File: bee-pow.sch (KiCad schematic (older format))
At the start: 41 parts, among them J1 Conn_01x02_Male, J2 Conn_01x02_Male, J3 Conn_01x02_Male, J4 Conn_01x02_Male, J5 Screw_Terminal_01x03, J6 Screw_Terminal_01x02, U1 L7805, U2 L7815, U3 L7915

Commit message: schematic and layout
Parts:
- removed D10, D12, D15: 1N4001, Diode_THT:D_A-405_P12.70mm_Horizontal, symbol Diode:1N4001
- removed D4, D7, D8: D_Schottky, Diode_THT:D_A-405_P10.16mm_Horizontal, symbol Device:D_Schottky
- removed J5: Screw_Terminal_01x03, TerminalBlock:TerminalBlock_bornier-3_P5.08mm, symbol Connector:Screw_Terminal_01x03
- removed J6: Screw_Terminal_01x02, TerminalBlock:TerminalBlock_bornier-2_P5.08mm, symbol Connector:Screw_Terminal_01x02
- added J5: Screw_Terminal_01x04, TerminalBlock:TerminalBlock_bornier-4_P5.08mm, symbol Connector:Screw_Terminal_01x04
- C7, C8, C9: footprint Capacitor_THT:CP_Radial_D10.0mm_P5.00mm -> Capacitor_THT:CP_Radial_D8.0mm_P2.50mm; order number RAD 220/35 -> RND 150ECR AZ
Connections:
- net labels added: U3_1
- wire segments 126 -> 125
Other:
- note removed: "Alternativ \nSMD oder DIL"
- moved on the sheet: D2, JP1

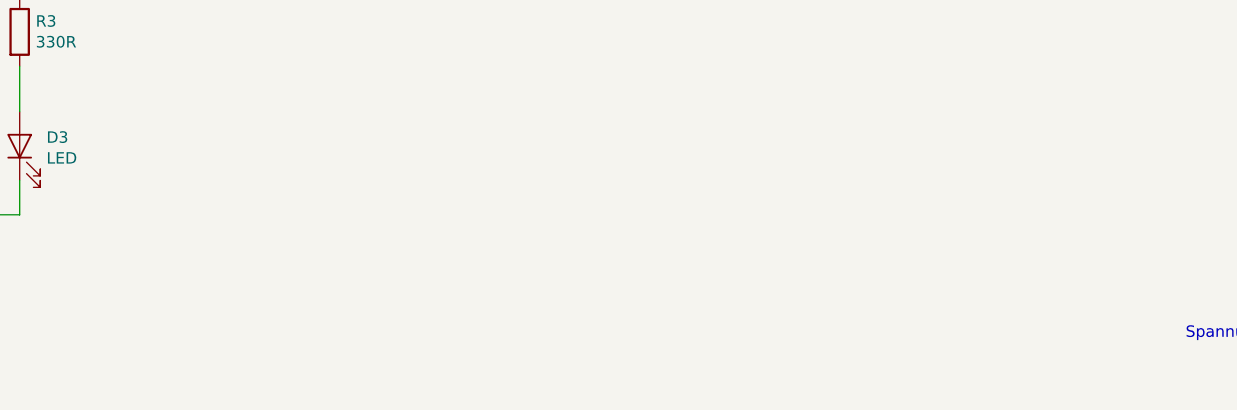
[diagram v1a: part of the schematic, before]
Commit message: Update labels and mounting holes.
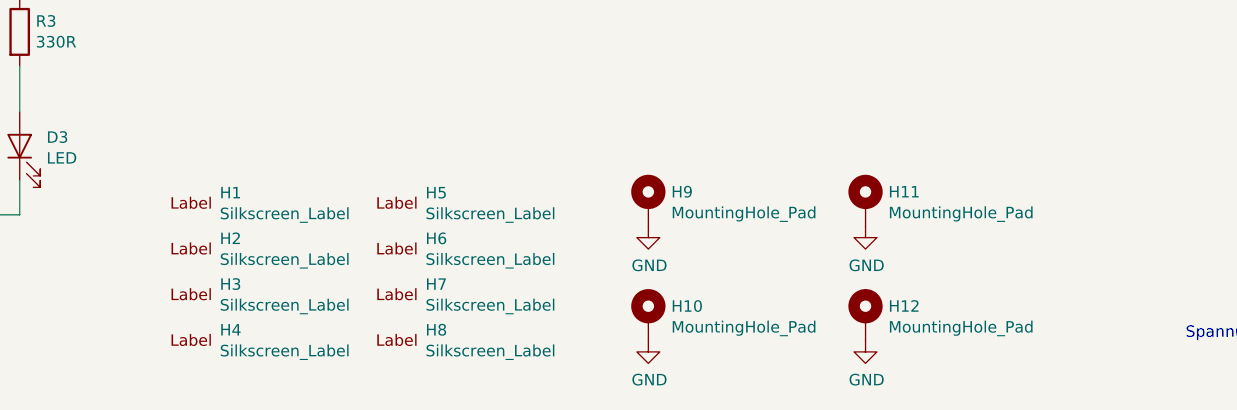
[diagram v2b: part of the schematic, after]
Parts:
- added H1, H2: Silkscreen_Label, Symbol-emt:Text_U_B+_Silkscreen, symbol Mechanical-emt:Silkscreen_Label
- added H10, H11, H12, H9: MountingHole_Pad, MountingHole:MountingHole_3.2mm_M3_ISO7380_Pad, symbol Mechanical:MountingHole_Pad
- added H3, H4: Silkscreen_Label, Symbol-emt:Text_U_B-_Silkscreen, symbol Mechanical-emt:Silkscreen_Label
- added H5, H6: Silkscreen_Label, Symbol-emt:Text_U_B2_Silkscreen, symbol Mechanical-emt:Silkscreen_Label
- added H7, H8: Silkscreen_Label, Symbol-emt:Symbol_GND_Silkscreen, symbol Mechanical-emt:Silkscreen_Label
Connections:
- net GND: now also H10.1, H11.1, H12.1, H9.1
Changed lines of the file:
@@
 Wire Wire Line
 	1800 6950 1800 6800
+$Comp
+L Mechanical-emt:Silkscreen_Label H1
+U 1 1 5CC84E73
+P 3000 6900
+F 0 "H1" H 3125 6945 50  0000 L CNN
+F 1 "Silkscreen_Label" H 3125 6854 50  0000 L CNN
+F 2 "Symbol-emt:Text_U_B+_Silkscreen" H 3000 6900 50  0001 C CNN
+F 3 "~" H 3000 6900 50  0001 C CNN
+	1    3000 6900
+	1    0    0    -1
+$EndComp
+$Comp
+L Mechanical-emt:Silkscreen_Label H2
+U 1 1 5CC86235
+P 3000 7100
+F 0 "H2" H 3125 7145 50  0000 L CNN
+F 1 "Silkscreen_Label" H 3125 7054 50  0000 L CNN
+F 2 "Symbol-emt:Text_U_B+_Silkscreen" H 3000 7100 50  0001 C CNN
+F 3 "~" H 3000 7100 50  0001 C CNN
+	1    3000 7100
+	1    0    0    -1
+$EndComp
+$Comp
+L Mechanical-emt:Silkscreen_Label H3
+U 1 1 5CC865CE
+P 3000 7300
+F 0 "H3" H 3125 7345 50  0000 L CNN
+F 1 "Silkscreen_Label" H 3125 7254 50  0000 L CNN
+F 2 "Symbol-emt:Text_U_B-_Silkscreen" H 3000 7300 50  0001 C CNN
+F 3 "~" H 3000 7300 50  0001 C CNN
+	1    3000 7300
+	1    0    0    -1
+$EndComp
+$Comp
+L Mechanical-emt:Silkscreen_Label H4
+U 1 1 5CC8C4D2
+P 3000 7500
+F 0 "H4" H 3125 7545 50  0000 L CNN
+F 1 "Silkscreen_Label" H 3125 7454 50  0000 L CNN
+F 2 "Symbol-emt:Text_U_B-_Silkscreen" H 3000 7500 50  0001 C CNN
+F 3 "~" H 3000 7500 50  0001 C CNN
+	1    3000 7500
+	1    0    0    -1
+$EndComp
+$Comp
+L Mechanical-emt:Silkscreen_Label H5
+U 1 1 5CC8C802
+P 3900 6900
+F 0 "H5" H 4025 6945 50  0000 L CNN
+F 1 "Silkscreen_Label" H 4025 6854 50  0000 L CNN
+F 2 "Symbol-emt:Text_U_B2_Silkscreen" H 3900 6900 50  0001 C CNN
+F 3 "~" H 3900 6900 50  0001 C CNN
+	1    3900 6900
+	1    0    0    -1
+$EndComp
+$Comp
+L Mechanical-emt:Silkscreen_Label H6
+U 1 1 5CC8CC95
+P 3900 7100
+F 0 "H6" H 4025 7145 50  0000 L CNN
+F 1 "Silkscreen_Label" H 4025 7054 50  0000 L CNN
+F 2 "Symbol-emt:Text_U_B2_Silkscreen" H 3900 7100 50  0001 C CNN
+F 3 "~" H 3900 7100 50  0001 C CNN
+	1    3900 7100
+	1    0    0    -1
+$EndComp
+$Comp
+L Mechanical-emt:Silkscreen_Label H7
+U 1 1 5CC8CECB
+P 3900 7300
+F 0 "H7" H 4025 7345 50  0000 L CNN
+F 1 "Silkscreen_Label" H 4025 7254 50  0000 L CNN
+F 2 "Symbol-emt:Symbol_GND_Silkscreen" H 3900 7300 50  0001 C CNN
+F 3 "~" H 3900 7300 50  0001 C CNN
+	1    3900 7300
+	1    0    0    -1
+$EndComp
+$Comp
+L Mechanical-emt:Silkscreen_Label H8
+U 1 1 5CC8D0ED
+P 3900 7500
+F 0 "H8" H 4025 7545 50  0000 L CNN
+F 1 "Silkscreen_Label" H 4025 7454 50  0000 L CNN
+F 2 "Symbol-emt:Symbol_GND_Silkscreen" H 3900 7500 50  0001 C CNN
+F 3 "~" H 3900 7500 50  0001 C CNN
+	1    3900 7500
+	1    0    0    -1
+$EndComp
+$Comp
+L Mechanical:MountingHole_Pad H9
+U 1 1 5CC913F6
+P 5000 6900
+F 0 "H9" H 5100 6949 50  0000 L CNN
+F 1 "MountingHole_Pad" H 5100 6858 50  0000 L CNN
+F 2 "MountingHole:MountingHole_3.2mm_M3_ISO7380_Pad" H 5000 6900 50  0001 C CNN
+F 3 "~" H 5000 6900 50  0001 C CNN
+	1    5000 6900
+	1    0    0    -1
+$EndComp
+$Comp
+L Mechanical:MountingHole_Pad H10
+U 1 1 5CC9212B
+P 5000 7400
+F 0 "H10" H 5100 7449 50  0000 L CNN
+F 1 "MountingHole_Pad" H 5100 7358 50  0000 L CNN
+F 2 "MountingHole:MountingHole_3.2mm_M3_ISO7380_Pad" H 5000 7400 50  0001 C CNN
+F 3 "~" H 5000 7400 50  0001 C CNN
+	1    5000 7400
+	1    0    0    -1
+$EndComp
+$Comp
+L Mechanical:MountingHole_Pad H11
+U 1 1 5CC92855
+P 5950 6900
+F 0 "H11" H 6050 6949 50  0000 L CNN
+F 1 "MountingHole_Pad" H 6050 6858 50  0000 L CNN
+F 2 "MountingHole:MountingHole_3.2mm_M3_ISO7380_Pad" H 5950 6900 50  0001 C CNN
+F 3 "~" H 5950 6900 50  0001 C CNN
+	1    5950 6900
+	1    0    0    -1
+$EndComp
+$Comp
+L Mechanical:MountingHole_Pad H12
+U 1 1 5CC92D13
+P 5950 7400
+F 0 "H12" H 6050 7449 50  0000 L CNN
+F 1 "MountingHole_Pad" H 6050 7358 50  0000 L CNN
+F 2 "MountingHole:MountingHole_3.2mm_M3_ISO7380_Pad" H 5950 7400 50  0001 C CNN
+F 3 "~" H 5950 7400 50  0001 C CNN
+	1    5950 7400
+	1    0    0    -1
+$EndComp
+$Comp
+L power:GND #PWR0107
+U 1 1 5CCA661C
+P 5000 7000
+F 0 "#PWR0107" H 5000 6750 50  0001 C CNN
+F 1 "GND" H 5005 6827 50  0000 C CNN
+F 2 "" H 5000 7000 50  0001 C CNN
+F 3 "" H 5000 7000 50  0001 C CNN
+	1    5000 7000
+	1    0    0    -1
+$EndComp
+$Comp
+L power:GND #PWR0108
+U 1 1 5CCA6E8E
+P 5950 7000
+F 0 "#PWR0108" H 5950 6750 50  0001 C CNN
+F 1 "GND" H 5955 6827 50  0000 C CNN
+F 2 "" H 5950 7000 50  0001 C CNN
+F 3 "" H 5950 7000 50  0001 C CNN
+	1    5950 7000
+	1    0    0    -1
+$EndComp
+$Comp
+L power:GND #PWR0109
+U 1 1 5CCA7769
+P 5000 7500
+F 0 "#PWR0109" H 5000 7250 50  0001 C CNN
+F 1 "GND" H 5005 7327 50  0000 C CNN
+F 2 "" H 5000 7500 50  0001 C CNN
+F 3 "" H 5000 7500 50  0001 C CNN
+	1    5000 7500
+	1    0    0    -1
+$EndComp
+$Comp
+L power:GND #PWR0110
+U 1 1 5CCA7B5F
+P 5950 7500
+F 0 "#PWR0110" H 5950 7250 50  0001 C CNN
+F 1 "GND" H 5955 7327 50  0000 C CNN
+F 2 "" H 5950 7500 50  0001 C CNN
+F 3 "" H 5950 7500 50  0001 C CNN
+	1    5950 7500
+	1    0    0    -1
+$EndComp
 $EndSCHEMATC

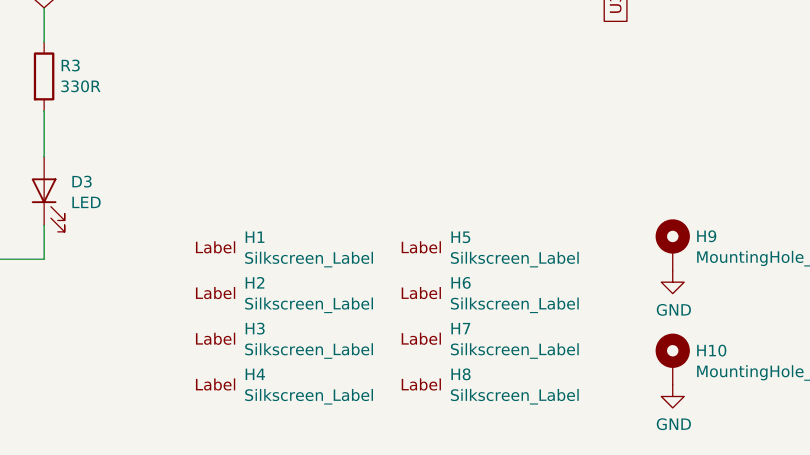
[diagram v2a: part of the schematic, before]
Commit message: Add text and logos.
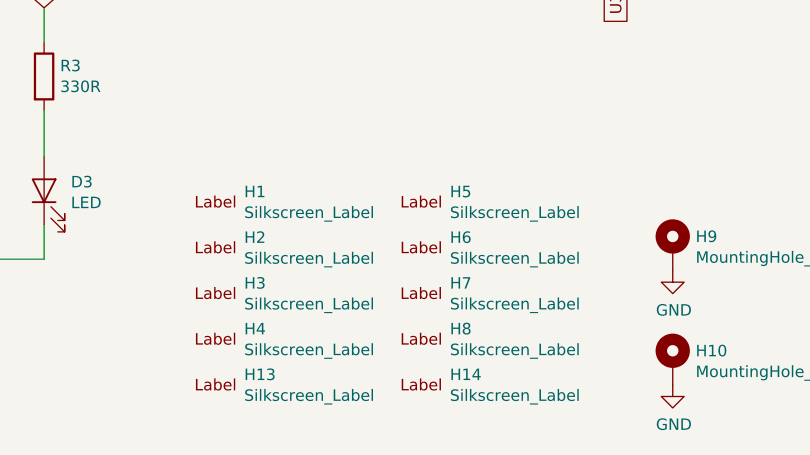
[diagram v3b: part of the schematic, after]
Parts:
- added H13: Silkscreen_Label, Symbol-emt:EMT-Logo_5.1x2.5mm_Silkscreen, symbol Mechanical-emt:Silkscreen_Label
- added H14: Silkscreen_Label, Symbol-emt:BEE-Logo_Silkscreen_small, symbol Mechanical-emt:Silkscreen_Label
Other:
- moved on the sheet: H1, H2, H3, H4, H5, H6, H7, H8
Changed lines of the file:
@@
 EESchema Schematic File Version 4
 LIBS:bee-pow-cache
-EELAYER 29 0
+EELAYER 26 0
 EELAYER END
 $Descr A4 11693 8268
@@
 L Mechanical-emt:Silkscreen_Label H1
 U 1 1 5CC84E73
+P 3000 6700
+F 0 "H1" H 3125 6745 50  0000 L CNN
+F 1 "Silkscreen_Label" H 3125 6654 50  0000 L CNN
+F 2 "Symbol-emt:Text_U_B+_Silkscreen" H 3000 6700 50  0001 C CNN
+F 3 "~" H 3000 6700 50  0001 C CNN
+	1    3000 6700
+	1    0    0    -1
+$EndComp
+$Comp
+L Mechanical-emt:Silkscreen_Label H2
+U 1 1 5CC86235
 P 3000 6900
-F 0 "H1" H 3125 6945 50  0000 L CNN
+F 0 "H2" H 3125 6945 50  0000 L CNN
 F 1 "Silkscreen_Label" H 3125 6854 50  0000 L CNN
 F 2 "Symbol-emt:Text_U_B+_Silkscreen" H 3000 6900 50  0001 C CNN
@@
 $EndComp
 $Comp
-L Mechanical-emt:Silkscreen_Label H2
-U 1 1 5CC86235
+L Mechanical-emt:Silkscreen_Label H3
+U 1 1 5CC865CE
 P 3000 7100
-F 0 "H2" H 3125 7145 50  0000 L CNN
+F 0 "H3" H 3125 7145 50  0000 L CNN
 F 1 "Silkscreen_Label" H 3125 7054 50  0000 L CNN
-F 2 "Symbol-emt:Text_U_B+_Silkscreen" H 3000 7100 50  0001 C CNN
+F 2 "Symbol-emt:Text_U_B-_Silkscreen" H 3000 7100 50  0001 C CNN
 F 3 "~" H 3000 7100 50  0001 C CNN
 	1    3000 7100
@@
 $EndComp
 $Comp
-L Mechanical-emt:Silkscreen_Label H3
-U 1 1 5CC865CE
+L Mechanical-emt:Silkscreen_Label H4
+U 1 1 5CC8C4D2
 P 3000 7300
-F 0 "H3" H 3125 7345 50  0000 L CNN
+F 0 "H4" H 3125 7345 50  0000 L CNN
 F 1 "Silkscreen_Label" H 3125 7254 50  0000 L CNN
 F 2 "Symbol-emt:Text_U_B-_Silkscreen" H 3000 7300 50  0001 C CNN
@@
 $EndComp
 $Comp
-L Mechanical-emt:Silkscreen_Label H4
-U 1 1 5CC8C4D2
-P 3000 7500
-F 0 "H4" H 3125 7545 50  0000 L CNN
-F 1 "Silkscreen_Label" H 3125 7454 50  0000 L CNN
-F 2 "Symbol-emt:Text_U_B-_Silkscreen" H 3000 7500 50  0001 C CNN
-F 3 "~" H 3000 7500 50  0001 C CNN
-	1    3000 7500
-	1    0    0    -1
-$EndComp
-$Comp
 L Mechanical-emt:Silkscreen_Label H5
 U 1 1 5CC8C802
+P 3900 6700
+F 0 "H5" H 4025 6745 50  0000 L CNN
+F 1 "Silkscreen_Label" H 4025 6654 50  0000 L CNN
+F 2 "Symbol-emt:Text_U_B2_Silkscreen" H 3900 6700 50  0001 C CNN
+F 3 "~" H 3900 6700 50  0001 C CNN
+	1    3900 6700
+	1    0    0    -1
+$EndComp
+$Comp
+L Mechanical-emt:Silkscreen_Label H6
+U 1 1 5CC8CC95
 P 3900 6900
-F 0 "H5" H 4025 6945 50  0000 L CNN
+F 0 "H6" H 4025 6945 50  0000 L CNN
 F 1 "Silkscreen_Label" H 4025 6854 50  0000 L CNN
 F 2 "Symbol-emt:Text_U_B2_Silkscreen" H 3900 6900 50  0001 C CNN
@@
 $EndComp
 $Comp
-L Mechanical-emt:Silkscreen_Label H6
-U 1 1 5CC8CC95
+L Mechanical-emt:Silkscreen_Label H7
+U 1 1 5CC8CECB
 P 3900 7100
-F 0 "H6" H 4025 7145 50  0000 L CNN
+F 0 "H7" H 4025 7145 50  0000 L CNN
 F 1 "Silkscreen_Label" H 4025 7054 50  0000 L CNN
-F 2 "Symbol-emt:Text_U_B2_Silkscreen" H 3900 7100 50  0001 C CNN
+F 2 "Symbol-emt:Symbol_GND_Silkscreen" H 3900 7100 50  0001 C CNN
 F 3 "~" H 3900 7100 50  0001 C CNN
 	1    3900 7100
@@
 $EndComp
 $Comp
-L Mechanical-emt:Silkscreen_Label H7
-U 1 1 5CC8CECB
+L Mechanical-emt:Silkscreen_Label H8
+U 1 1 5CC8D0ED
 P 3900 7300
-F 0 "H7" H 4025 7345 50  0000 L CNN
+F 0 "H8" H 4025 7345 50  0000 L CNN
 F 1 "Silkscreen_Label" H 4025 7254 50  0000 L CNN
 F 2 "Symbol-emt:Symbol_GND_Silkscreen" H 3900 7300 50  0001 C CNN
 F 3 "~" H 3900 7300 50  0001 C CNN
 	1    3900 7300
-	1    0    0    -1
-$EndComp
-$Comp
-L Mechanical-emt:Silkscreen_Label H8
-U 1 1 5CC8D0ED
-P 3900 7500
-F 0 "H8" H 4025 7545 50  0000 L CNN
-F 1 "Silkscreen_Label" H 4025 7454 50  0000 L CNN
-F 2 "Symbol-emt:Symbol_GND_Silkscreen" H 3900 7500 50  0001 C CNN
-F 3 "~" H 3900 7500 50  0001 C CNN
-	1    3900 7500
 	1    0    0    -1
 $EndComp
@@
 	1    0    0    -1
 $EndComp
+$Comp
+L Mechanical-emt:Silkscreen_Label H13
+U 1 1 5CCCD487
+P 3000 7500
+F 0 "H13" H 3125 7545 50  0000 L CNN
+F 1 "Silkscreen_Label" H 3125 7454 50  0000 L CNN
+F 2 "Symbol-emt:EMT-Logo_5.1x2.5mm_Silkscreen" H 3000 7500 50  0001 C CNN
+F 3 "~" H 3000 7500 50  0001 C CNN
+	1    3000 7500
+	1    0    0    -1
+$EndComp
+$Comp
+L Mechanical-emt:Silkscreen_Label H14
+U 1 1 5CCCD4F9
+P 3900 7500
+F 0 "H14" H 4025 7545 50  0000 L CNN
+F 1 "Silkscreen_Label" H 4025 7454 50  0000 L CNN
+F 2 "Symbol-emt:BEE-Logo_Silkscreen_small" H 3900 7500 50  0001 C CNN
+F 3 "~" H 3900 7500 50  0001 C CNN
+	1    3900 7500
+	1    0    0    -1
+$EndComp

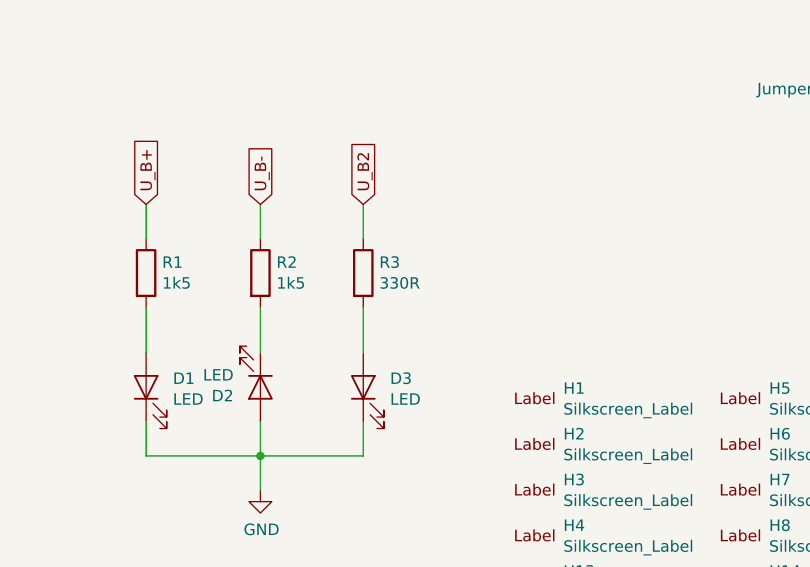
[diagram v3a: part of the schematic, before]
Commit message: Add part numbers.
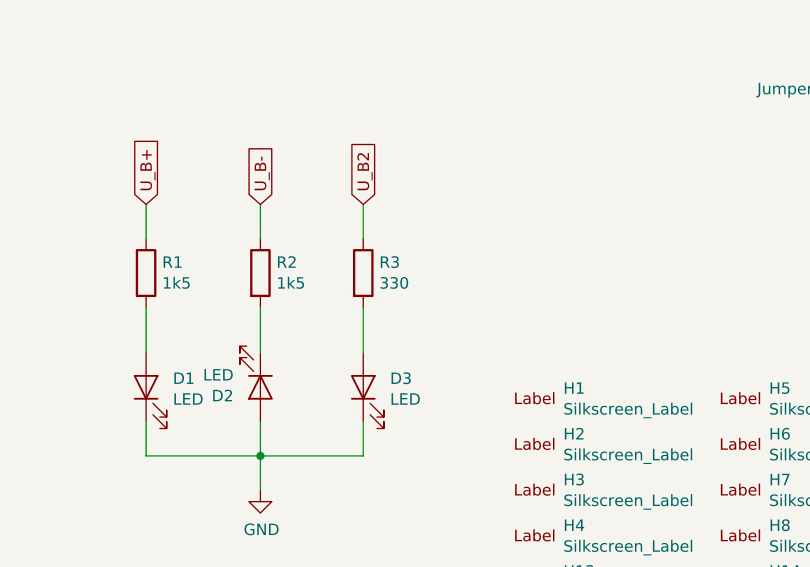
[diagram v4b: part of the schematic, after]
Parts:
- C1, C2, C3: Reichelt Part No (none) -> RND 1500805B3342; order number RND 1500805B3342 -> (none)
- C4, C5, C6: Reichelt Part No (none) -> X7R-G0805 100N; order number KEM X7R0805 100N -> (none)
- C7, C8, C9: Reichelt Part No (none) -> RND 150ECR BA; order number RND 150ECR AZ -> (none)
- D1, D2, D3: Reichelt Part No (none) -> OSO LGR971; order number OSO LGR971 -> (none)
- D11, D13, D14, D16, D17, D18: Reichelt Part No (none) -> 1N 4001 SMD; order number 1N 4001 SMD -> (none)
- D5, D6, D9: Reichelt Part No (none) -> STPS 2L40U STM; order number STPS 2L40U STM -> (none)
- J1, J2, J3, J4: Reichelt Part No (none) -> RND 205-00623
- J5: Reichelt Part No (none) -> RND 205-00014
- JP1, JP2: Reichelt Part No (none) -> RND 205-00624
- R1, R2: Reichelt Part No (none) -> RND 1550805 CN; order number RND 1550805 CN -> (none)
- R3: value 330R -> 330; Reichelt Part No (none) -> RND 0805 1 330; order number RND 0805 1 330 -> (none)
- U1: Reichelt Part No (none) -> L7805CV-DG STM
- U2: Reichelt Part No (none) -> L7815CV STM; order number L7815CV STM -> (none)
- U3: Reichelt Part No (none) -> L7915CV STM

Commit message: Relabel as bee specific.
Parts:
- H1, H2: footprint Symbol-emt:Text_U_B+_Silkscreen -> Symbol-bee:Text_U_B+_Silkscreen; symbol Mechanical-emt:Silkscreen_Label -> Mechanical-bee:Silkscreen_Label
- H13: footprint Symbol-emt:EMT-Logo_5.1x2.5mm_Silkscreen -> Symbol-bee:EMT-Logo_5.1x2.5mm_Silkscreen; symbol Mechanical-emt:Silkscreen_Label -> Mechanical-bee:Silkscreen_Label
- H14: footprint Symbol-emt:BEE-Logo_Silkscreen_small -> Symbol-bee:BEE-Logo_Silkscreen_small; symbol Mechanical-emt:Silkscreen_Label -> Mechanical-bee:Silkscreen_Label
- H3, H4: footprint Symbol-emt:Text_U_B-_Silkscreen -> Symbol-bee:Text_U_B-_Silkscreen; symbol Mechanical-emt:Silkscreen_Label -> Mechanical-bee:Silkscreen_Label
- H5, H6: footprint Symbol-emt:Text_U_B2_Silkscreen -> Symbol-bee:Text_U_B2_Silkscreen; symbol Mechanical-emt:Silkscreen_Label -> Mechanical-bee:Silkscreen_Label
- H7, H8: footprint Symbol-emt:Symbol_GND_Silkscreen -> Symbol-bee:Symbol_GND_Silkscreen; symbol Mechanical-emt:Silkscreen_Label -> Mechanical-bee:Silkscreen_Label
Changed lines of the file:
@@
 	1800 6950 1800 6800
 $Comp
-L Mechanical-emt:Silkscreen_Label H1
+L Mechanical-bee:Silkscreen_Label H1
 U 1 1 5CC84E73
 P 3000 6700
 F 0 "H1" H 3125 6745 50  0000 L CNN
 F 1 "Silkscreen_Label" H 3125 6654 50  0000 L CNN
-F 2 "Symbol-emt:Text_U_B+_Silkscreen" H 3000 6700 50  0001 C CNN
+F 2 "Symbol-bee:Text_U_B+_Silkscreen" H 3000 6700 50  0001 C CNN
 F 3 "~" H 3000 6700 50  0001 C CNN
 	1    3000 6700
@@
 $EndComp
 $Comp
-L Mechanical-emt:Silkscreen_Label H2
+L Mechanical-bee:Silkscreen_Label H2
 U 1 1 5CC86235
 P 3000 6900
 F 0 "H2" H 3125 6945 50  0000 L CNN
 F 1 "Silkscreen_Label" H 3125 6854 50  0000 L CNN
-F 2 "Symbol-emt:Text_U_B+_Silkscreen" H 3000 6900 50  0001 C CNN
+F 2 "Symbol-bee:Text_U_B+_Silkscreen" H 3000 6900 50  0001 C CNN
 F 3 "~" H 3000 6900 50  0001 C CNN
 	1    3000 6900
@@
 $EndComp
 $Comp
-L Mechanical-emt:Silkscreen_Label H3
+L Mechanical-bee:Silkscreen_Label H3
 U 1 1 5CC865CE
 P 3000 7100
 F 0 "H3" H 3125 7145 50  0000 L CNN
 F 1 "Silkscreen_Label" H 3125 7054 50  0000 L CNN
-F 2 "Symbol-emt:Text_U_B-_Silkscreen" H 3000 7100 50  0001 C CNN
+F 2 "Symbol-bee:Text_U_B-_Silkscreen" H 3000 7100 50  0001 C CNN
 F 3 "~" H 3000 7100 50  0001 C CNN
 	1    3000 7100
@@
 $EndComp
 $Comp
-L Mechanical-emt:Silkscreen_Label H4
+L Mechanical-bee:Silkscreen_Label H4
 U 1 1 5CC8C4D2
 P 3000 7300
 F 0 "H4" H 3125 7345 50  0000 L CNN
 F 1 "Silkscreen_Label" H 3125 7254 50  0000 L CNN
-F 2 "Symbol-emt:Text_U_B-_Silkscreen" H 3000 7300 50  0001 C CNN
+F 2 "Symbol-bee:Text_U_B-_Silkscreen" H 3000 7300 50  0001 C CNN
 F 3 "~" H 3000 7300 50  0001 C CNN
 	1    3000 7300
@@
 $EndComp
 $Comp
-L Mechanical-emt:Silkscreen_Label H5
+L Mechanical-bee:Silkscreen_Label H5
 U 1 1 5CC8C802
 P 3900 6700
 F 0 "H5" H 4025 6745 50  0000 L CNN
 F 1 "Silkscreen_Label" H 4025 6654 50  0000 L CNN
-F 2 "Symbol-emt:Text_U_B2_Silkscreen" H 3900 6700 50  0001 C CNN
+F 2 "Symbol-bee:Text_U_B2_Silkscreen" H 3900 6700 50  0001 C CNN
 F 3 "~" H 3900 6700 50  0001 C CNN
 	1    3900 6700
@@
 $EndComp
 $Comp
-L Mechanical-emt:Silkscreen_Label H6
+L Mechanical-bee:Silkscreen_Label H6
 U 1 1 5CC8CC95
 P 3900 6900
 F 0 "H6" H 4025 6945 50  0000 L CNN
 F 1 "Silkscreen_Label" H 4025 6854 50  0000 L CNN
-F 2 "Symbol-emt:Text_U_B2_Silkscreen" H 3900 6900 50  0001 C CNN
+F 2 "Symbol-bee:Text_U_B2_Silkscreen" H 3900 6900 50  0001 C CNN
 F 3 "~" H 3900 6900 50  0001 C CNN
 	1    3900 6900
@@
 $EndComp
 $Comp
-L Mechanical-emt:Silkscreen_Label H7
+L Mechanical-bee:Silkscreen_Label H7
 U 1 1 5CC8CECB
 P 3900 7100
 F 0 "H7" H 4025 7145 50  0000 L CNN
 F 1 "Silkscreen_Label" H 4025 7054 50  0000 L CNN
-F 2 "Symbol-emt:Symbol_GND_Silkscreen" H 3900 7100 50  0001 C CNN
+F 2 "Symbol-bee:Symbol_GND_Silkscreen" H 3900 7100 50  0001 C CNN
 F 3 "~" H 3900 7100 50  0001 C CNN
 	1    3900 7100
@@
 $EndComp
 $Comp
-L Mechanical-emt:Silkscreen_Label H8
+L Mechanical-bee:Silkscreen_Label H8
 U 1 1 5CC8D0ED
 P 3900 7300
 F 0 "H8" H 4025 7345 50  0000 L CNN
 F 1 "Silkscreen_Label" H 4025 7254 50  0000 L CNN
-F 2 "Symbol-emt:Symbol_GND_Silkscreen" H 3900 7300 50  0001 C CNN
+F 2 "Symbol-bee:Symbol_GND_Silkscreen" H 3900 7300 50  0001 C CNN
 F 3 "~" H 3900 7300 50  0001 C CNN
 	1    3900 7300
@@
 $EndComp
 $Comp
-L Mechanical-emt:Silkscreen_Label H13
+L Mechanical-bee:Silkscreen_Label H13
 U 1 1 5CCCD487
 P 3000 7500
 F 0 "H13" H 3125 7545 50  0000 L CNN
 F 1 "Silkscreen_Label" H 3125 7454 50  0000 L CNN
-F 2 "Symbol-emt:EMT-Logo_5.1x2.5mm_Silkscreen" H 3000 7500 50  0001 C CNN
+F 2 "Symbol-bee:EMT-Logo_5.1x2.5mm_Silkscreen" H 3000 7500 50  0001 C CNN
 F 3 "~" H 3000 7500 50  0001 C CNN
 	1    3000 7500
@@
 $EndComp
 $Comp
-L Mechanical-emt:Silkscreen_Label H14
+L Mechanical-bee:Silkscreen_Label H14
 U 1 1 5CCCD4F9
 P 3900 7500
 F 0 "H14" H 4025 7545 50  0000 L CNN
 F 1 "Silkscreen_Label" H 4025 7454 50  0000 L CNN
-F 2 "Symbol-emt:BEE-Logo_Silkscreen_small" H 3900 7500 50  0001 C CNN
+F 2 "Symbol-bee:BEE-Logo_Silkscreen_small" H 3900 7500 50  0001 C CNN
 F 3 "~" H 3900 7500 50  0001 C CNN
 	1    3900 7500
